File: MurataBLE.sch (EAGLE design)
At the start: 46 parts, among them CON1 C-2235, IC1 I-5448, IC3 74LVC1G00DBV, Q1 FC-135 32.7680KA-AG3, SW1 P8073, SW2 P8073, SW3 P8073, U1 IC_BLE_LBCA2HNZYZ-711, X1 C-04397

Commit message: update eagle version = 7.5.0; library update
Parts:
- CON1: device mylib:CON_USB -> mylib:CON_USB_MINIB
- IC1: device mylib:IC_LDO_XX1117_5 -> mylib:LDO5_3.3_SOT23
- Q1: device mylib:CLOCK_CRYSTAL_FC-135 -> mylib:CRYSTAL2_32.768K_FC-135
- Q2: device mylib:CLOCK_CRYSTAL_4_3225 -> mylib:CRYSTAL4_12M_3225
- R11, R5: value 75/1005 -> (none); device mylib:R_US_75R_1005 -> mylib:R_US_1.0K_1005
- R4: value 270/1005 -> (none); device mylib:R_US_270R_1005 -> mylib:R_US_1.0K_1005
- SW1, SW2: value P8073 -> (none); device mylib:SW_TACTSW_2PP8073 -> mylib:TACTSW2_BK_P807X
- SW3: value P8073 -> (none); device mylib:SW_TACTSW_2PP8073 -> mylib:TACTSW2_WH_P807X
- U1: value IC_BLE_LBCA2HNZYZ-711 -> LBCA2HNZYZ-711; device mylib:IC_BLE_LBCA2HNZYZ-711 -> mylib:LBCA2HNZYZ-711
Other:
- moved on the sheet: CON1
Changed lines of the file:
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@@
 <?xml version="1.0" encoding="utf-8"?>
 <!DOCTYPE eagle SYSTEM "eagle.dtd">
-<eagle version="6.5.0">
+<eagle version="7.5.0">
 <drawing>
 <settings>
@@
 <grid distance="0.1" unitdist="inch" unit="inch" style="lines" multiple="1" display="no" altdistance="0.01" altunitdist="inch" altunit="inch"/>
 <layers>
-<layer number="1" name="Top" color="4" fill="1" visible="no" active="no"/>
+<layer number="1" name="Top" color="4" fill="0" visible="no" active="no"/>
 <layer number="2" name="Route2" color="1" fill="3" visible="no" active="no"/>
 <layer number="3" name="Route3" color="4" fill="3" visible="no" active="no"/>
 <layer number="14" name="Route14" color="1" fill="6" visible="no" active="no"/>
 <layer number="15" name="Route15" color="4" fill="6" visible="no" active="no"/>
-<layer number="16" name="Bottom" color="1" fill="1" visible="no" active="no"/>
+<layer number="16" name="Bottom" color="9" fill="0" visible="no" active="no"/>
 <layer number="17" name="Pads" color="2" fill="1" visible="no" active="no"/>
 <layer number="18" name="Vias" color="2" fill="1" visible="no" active="no"/>
@@
 <layer number="44" name="Drills" color="7" fill="1" visible="no" active="no"/>
 <layer number="45" name="Holes" color="7" fill="1" visible="no" active="no"/>
-<layer number="46" name="Milling" color="3" fill="1" visible="no" active="no"/>
+<layer number="46" name="Milling" color="3" fill="0" visible="no" active="no"/>
 <layer number="47" name="Measures" color="7" fill="1" visible="no" active="no"/>
 <layer number="48" name="Document" color="7" fill="1" visible="no" active="no"/>
@@
 <parts>
 <part name="FRAME1" library="frames" deviceset="A4L-LOC" device=""/>
-<part name="U1" library="mylib" deviceset="IC_BLE_LBCA2HNZYZ-711" device=""/>
+<part name="U1" library="mylib" deviceset="LBCA2HNZYZ-711" device=""/>
 <part name="SUPPLY1" library="mylib" deviceset="GND" device=""/>
-<part name="Q1" library="mylib" deviceset="CLOCK_CRYSTAL" device="_FC-135" value="FC-135 32.7680KA-AG3"/>
+<part name="Q1" library="mylib" deviceset="CRYSTAL2_*" device="_FC-135" technology="32.768K" value="FC-135 32.7680KA-AG3"/>
 <part name="C2" library="mylib" deviceset="C_SMD_*" device="_1005" technology="0.1U" value="0.1u/1005"/>
-<part name="SW1" library="mylib" deviceset="SW_TACTSW_2P" device="P8073" value="P8073"/>
+<part name="SW1" library="mylib" deviceset="TACTSW2_*" device="_P807X" technology="BK"/>
 <part name="PCB1" library="dp_pcb" deviceset="PCB_DP_RECTANGLE" device="-31X50"/>
 <part name="R1" library="mylib" deviceset="R_US_*" device="_1005" technology="10K" value="10k/1005"/>
 <part name="IC2" library="mylib" deviceset="IC_LPC11U35IF" device="&quot;&quot;"/>
-<part name="CON1" library="mylib" deviceset="CON_USB" device="" value="C-2235"/>
+<part name="CON1" library="mylib" deviceset="CON_USB" device="_MINIB" value="C-2235"/>
 <part name="C1" library="mylib" deviceset="C_SMD_*" device="_1608" technology="1.0U" value="1u/1608"/>
 <part name="C3" library="mylib" deviceset="C_SMD_*" device="_1608" technology="1.0U" value="1u/1608"/>
@@
 <part name="R3" library="mylib" deviceset="R_US_*" device="_1005" technology="33R" value="33/1005"/>
 <part name="SUPPLY7" library="mylib" deviceset="GND" device=""/>
-<part name="SW2" library="mylib" deviceset="SW_TACTSW_2P" device="P8073" value="P8073"/>
-<part name="SW3" library="mylib" deviceset="SW_TACTSW_2P" device="P8073" value="P8073"/>
+<part name="SW2" library="mylib" deviceset="TACTSW2_*" device="_P807X" technology="BK"/>
+<part name="SW3" library="mylib" deviceset="TACTSW2_*" device="_P807X" technology="WH"/>
 <part name="SUPPLY8" library="mylib" deviceset="GND" device=""/>
 <part name="SUPPLY9" library="mylib" deviceset="GND" device=""/>
@@
 <part name="R8" library="mylib" deviceset="R_US_*" device="_1005" technology="10K" value="10k/1005"/>
 <part name="R9" library="mylib" deviceset="R_US_*" device="_1005" technology="10K" value="10k/1005"/>
-<part name="IC1" library="mylib" deviceset="IC_LDO_XX1117_5" device="" value="I-5448"/>
+<part name="IC1" library="mylib" deviceset="LDO5_*" device="_SOT23" technology="3.3" value="I-5448"/>
 <part name="C4" library="mylib" deviceset="C_SMD_*" device="_1005" technology="0.1U" value="0.1u/1005"/>
 <part name="SUPPLY10" library="mylib" deviceset="GND" device=""/>
@@
 <part name="R10" library="mylib" deviceset="R_US_*" device="_1005" technology="1.5K" value="1.5k/1005"/>
 <part name="IC3" library="74xx-little-us_local" deviceset="74*1G00" device="DBV" technology="LVC" value="74LVC1G00DBV"/>
-<part name="R4" library="mylib" deviceset="R_US_*" device="_1005" technology="270R" value="270/1005"/>
-<part name="R5" library="mylib" deviceset="R_US_*" device="_1005" technology="75R" value="75/1005"/>
-<part name="R11" library="mylib" deviceset="R_US_*" device="_1005" technology="75R" value="75/1005"/>
+<part name="R4" library="mylib" deviceset="R_US_*" device="_1005" technology="1.0K"/>
+<part name="R5" library="mylib" deviceset="R_US_*" device="_1005" technology="1.0K"/>
+<part name="R11" library="mylib" deviceset="R_US_*" device="_1005" technology="1.0K"/>
 <part name="SUPPLY16" library="mylib" deviceset="GND" device=""/>
 <part name="LED1" library="mylib" deviceset="LED_3SEG" device=""/>
@@
 <part name="TP10" library="mylib" deviceset="TESTPAD" device="_F" value="TESTPAD_F"/>
 <part name="TP11" library="mylib" deviceset="TESTPAD" device="_F" value="TESTPAD_F"/>
-<part name="Q2" library="mylib" deviceset="CLOCK_CRYSTAL_4" device="_3225"/>
+<part name="Q2" library="mylib" deviceset="CRYSTAL4_*" device="_3225" technology="12M"/>
 </parts>
 <sheets>
 <sheet>
 <plain>
-<text x="226.06" y="25.4" size="5.08" layer="94">rev 0.3</text>
+<text x="162.56" y="5.08" size="5.08" layer="94">rev 0.3</text>
 <text x="190.5" y="96.52" size="1.778" layer="91">Vf@5mA:
 (R) = 1.9V
@@
 <text x="233.68" y="139.7" size="1.778" layer="94">P0_0 -&gt; TGT_TX
 P0_1 &lt;- TGT_RX</text>
-<text x="226.06" y="20.32" size="2.54" layer="94">CC-BY-SA</text>
+<text x="162.56" y="20.32" size="2.54" layer="94">CC-BY-SA</text>
 <text x="177.8" y="38.1" size="1.778" layer="91">FIDUCIALS</text>
 <circle x="185.42" y="43.18" radius="11.359225" width="0.1524" layer="91"/>
@@
 <instance part="Q1" gate="G$1" x="190.5" y="127"/>
 <instance part="C2" gate="G$1" x="180.34" y="137.16"/>
-<instance part="SW1" gate="G$1" x="76.2" y="142.24"/>
+<instance part="SW1" gate="G$1" x="76.2" y="142.24">
+<attribute name="AKIZUKI" x="81.28" y="137.16" size="0.8128" layer="96" rot="R90" display="both"/>
+</instance>
 <instance part="PCB1" gate="G$1" x="12.7" y="10.16"/>
 <instance part="R1" gate="G$1" x="78.74" y="162.56" rot="R270"/>
@@
 <instance part="R3" gate="G$1" x="55.88" y="93.98"/>
 <instance part="SUPPLY7" gate="GND" x="96.52" y="139.7"/>
-<instance part="SW2" gate="G$1" x="160.02" y="139.7"/>
-<instance part="SW3" gate="G$1" x="139.7" y="139.7"/>
+<instance part="SW2" gate="G$1" x="160.02" y="139.7">
+<attribute name="AKIZUKI" x="165.1" y="134.62" size="0.8128" layer="96" rot="R90" display="both"/>
+</instance>
+<instance part="SW3" gate="G$1" x="139.7" y="139.7">
+<attribute name="AKIZUKI" x="144.78" y="134.62" size="0.8128" layer="96" rot="R90" display="both"/>
+</instance>
 <instance part="SUPPLY8" gate="GND" x="142.24" y="132.08"/>
 <instance part="SUPPLY9" gate="GND" x="162.56" y="132.08"/>
@@
 <instance part="R8" gate="G$1" x="162.56" y="160.02" rot="R270"/>
 <instance part="R9" gate="G$1" x="99.06" y="106.68"/>
-<instance part="IC1" gate="G$1" x="33.02" y="162.56"/>
+<instance part="IC1" gate="G$1" x="33.02" y="162.56">
+<attribute name="AKIZUKI" x="27.94" y="162.56" size="0.8128" layer="96" display="both"/>
+</instance>
 <instance part="C4" gate="G$1" x="124.46" y="165.1"/>
 <instance part="SUPPLY10" gate="GND" x="124.46" y="144.78"/>

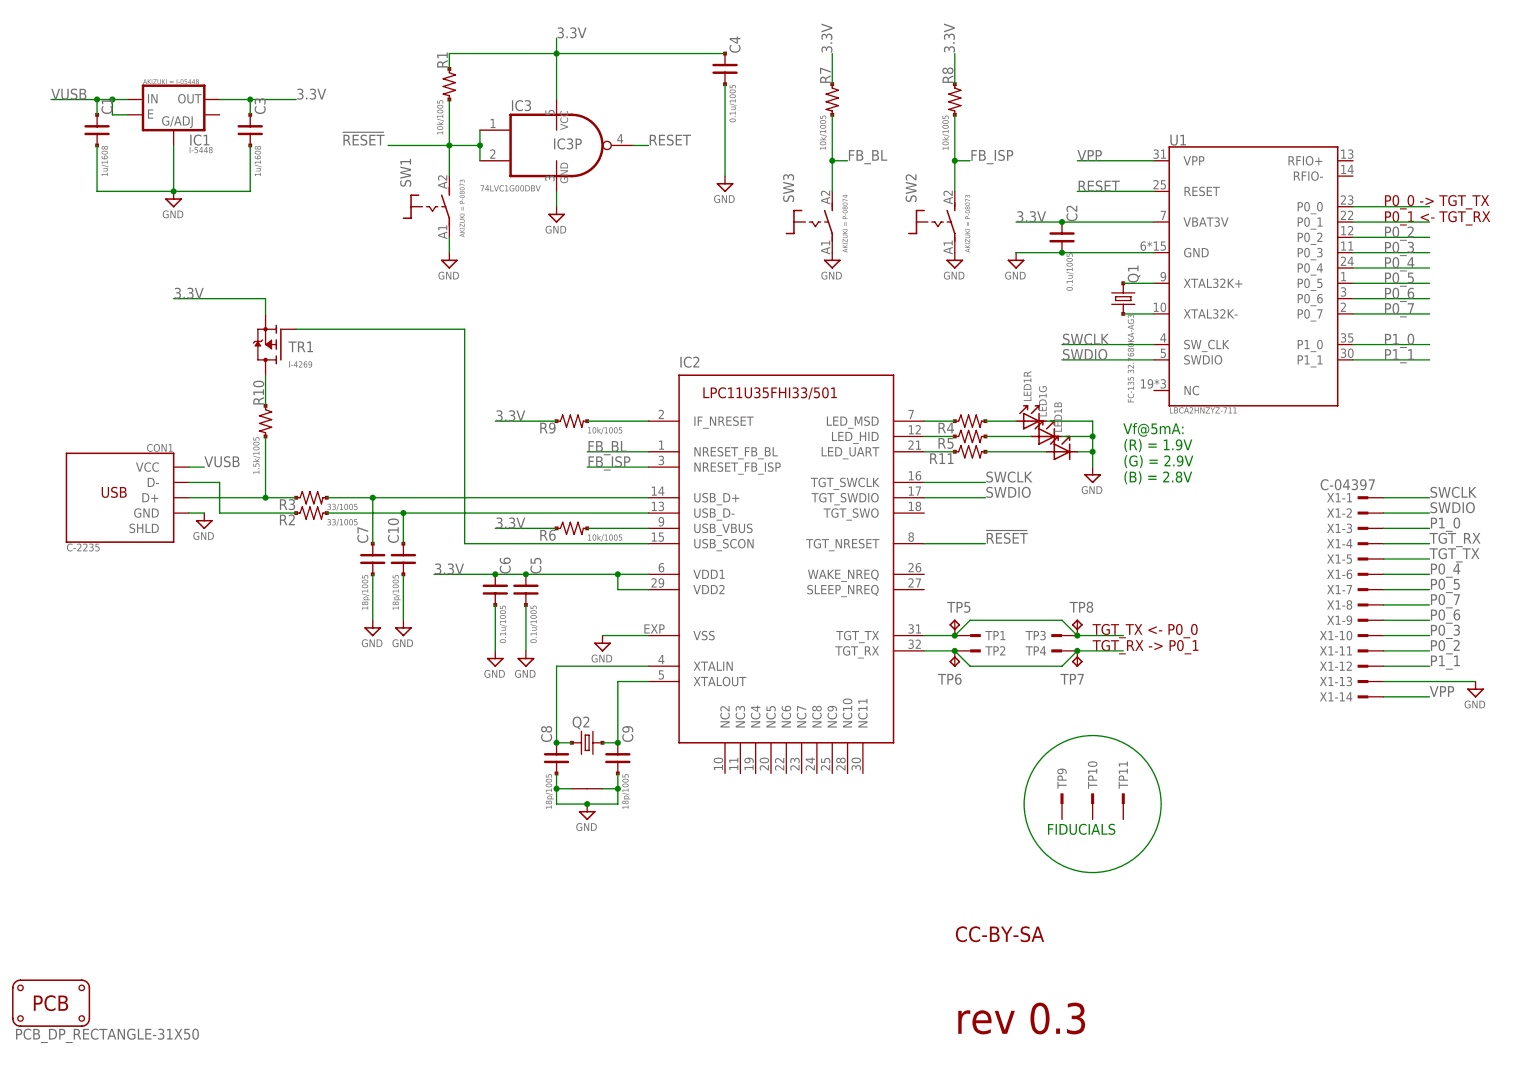
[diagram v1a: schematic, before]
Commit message: [ USB ] add IC4/5
replace IC2 symbol; change R11 connection
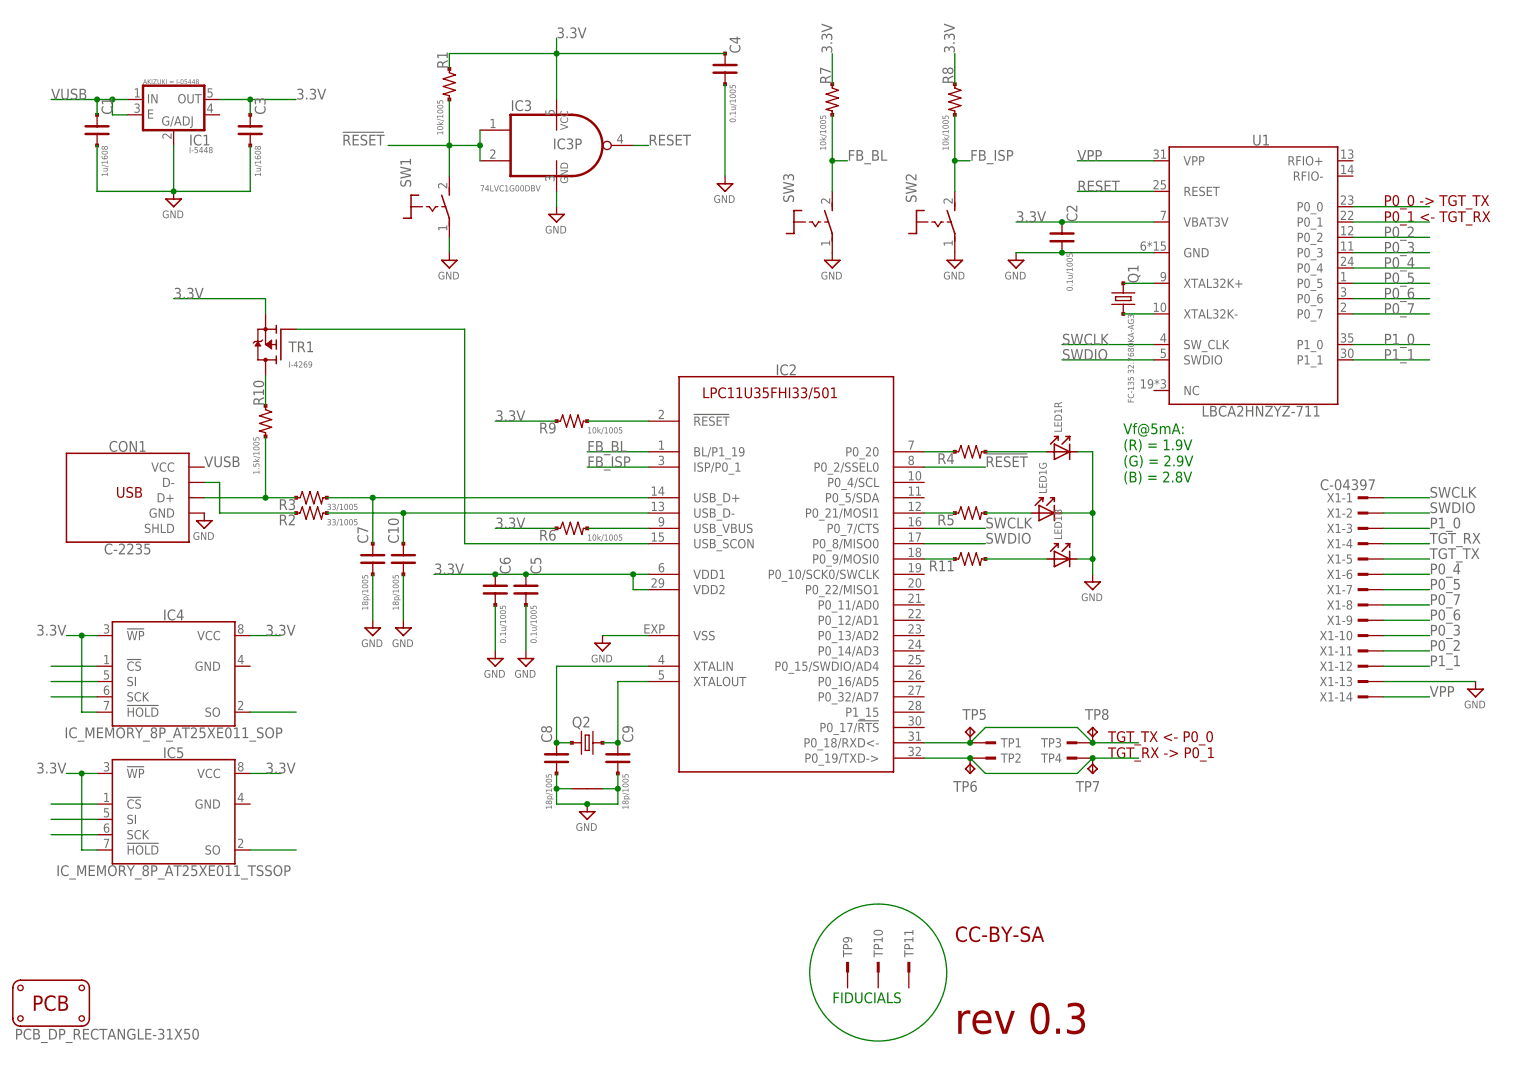
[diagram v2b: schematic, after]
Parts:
- added IC4: IC_MEMORY_8P_AT25XE011_SOP, mylib:IC_MEMORY_8P_AT25XE011_SOP
- added IC5: IC_MEMORY_8P_AT25XE011_TSSOP, mylib:IC_MEMORY_8P_AT25XE011_TSSOP
- IC2: device mylib:IC_LPC11U35IF"" -> mylib:IC_LPC11U35_QFN33_5X5
- SW1, SW2: device mylib:TACTSW2_BK_P807X -> mylib:TACTSW2_FSM2JMTR
- SW3: device mylib:TACTSW2_WH_P807X -> mylib:TACTSW2_FSM2JMTR
- TP1, TP2, TP3, TP4: value TESTPAD -> (none)
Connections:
- new net N$15: IC4.!CS
- new net N$16: IC4.SI
- new net N$17: IC4.SCK
- new net N$23: IC4.SO
- new net N$25: IC5.!CS
- new net N$26: IC5.SI
- new net N$27: IC5.SCK
- new net N$28: IC5.SO
- net !RESET!: now also IC2.P0_2/SSEL0; no longer IC2.TGT_NRESET
- net 3.3V: now also IC4.VCC, IC5.!HOLD, IC5.!WP, IC5.VCC
- net FB_BL: now also IC2.BL/P1_19; no longer IC2.NRESET_FB_BL
- net FB_ISP: now also IC2.ISP/P0_1; no longer IC2.NRESET_FB_ISP
- net N$10: now also IC2.P0_9/MOSI0; no longer IC2.LED_UART
- net N$5: now also IC2.!RESET!; no longer IC2.IF_NRESET
- net N$8: now also IC2.P0_20; no longer IC2.LED_MSD
- net N$9: now also IC2.P0_21/MOSI1; no longer IC2.LED_HID
- net SWCLK: now also IC2.P0_7/CTS; no longer IC2.TGT_SWCLK
- net SWDIO: now also IC2.P0_8/MISO0; no longer IC2.TGT_SWDIO
- net TGT_RX: now also IC2.P0_19/TXD->; no longer IC2.TGT_RX
- net TGT_TX: now also IC2.P0_18/RXD<-; no longer IC2.TGT_TX
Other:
- moved on the sheet: CON1, LED1B, LED1G, LED1R, R11, R4, R5, TP1, TP10, TP11, TP2, TP3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
